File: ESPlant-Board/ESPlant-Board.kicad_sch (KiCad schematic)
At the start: 31 parts, among them J1 Conn_01x05, U1 ESP32-C6-MINI-1/U, U3 Reset, U4 Boot, U5 Temp/Humid-Sensor, U6 Light sensor, U7 AMS1117-3_3, U8 MK-12C02-G025

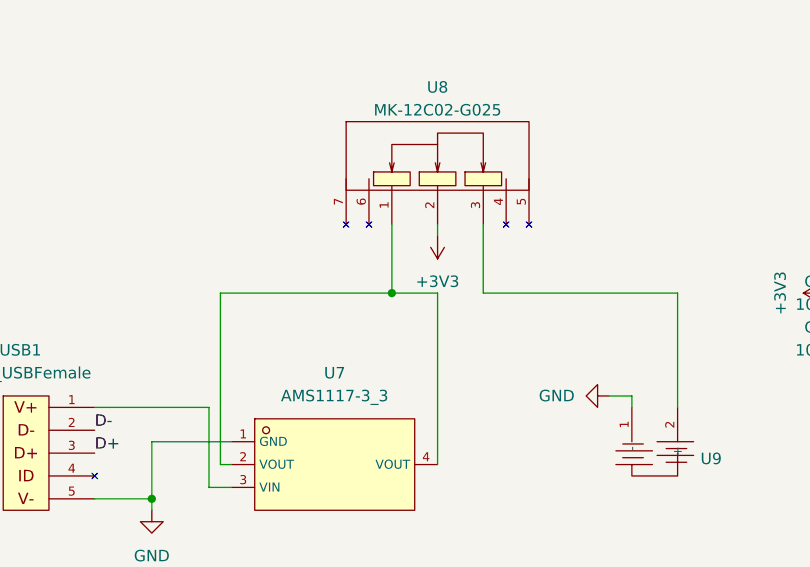
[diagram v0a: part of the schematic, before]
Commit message: Case: Add v2 case with improved folder structure
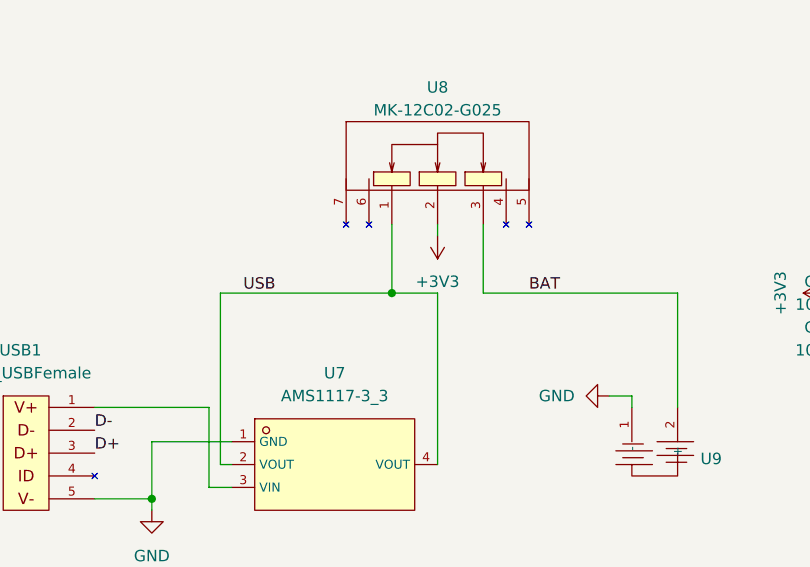
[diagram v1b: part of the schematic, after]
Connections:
- net USB: now reaches U7.2 (VOUT), U7.4 (VOUT), U8.1
- net BAT: now reaches U8.3, U9.2 (+)
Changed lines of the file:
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@@
+    (effects (font (size 1.27 1.27)) (justify left bottom))
+  )
+  (label "USB" (at 48.26 165.1 0) (fields_autoplaced)
     (effects (font (size 1.27 1.27)) (justify left bottom))
   )
@@
     (effects (font (size 1.27 1.27)) (justify right bottom))
   )
+  (label "BAT" (at 80.01 165.1 0) (fields_autoplaced)
+    (effects (font (size 1.27 1.27)) (justify left bottom))
+  )
   (symbol (lib_id "Device:C") (at 74.93 115.57 0) (unit 1)

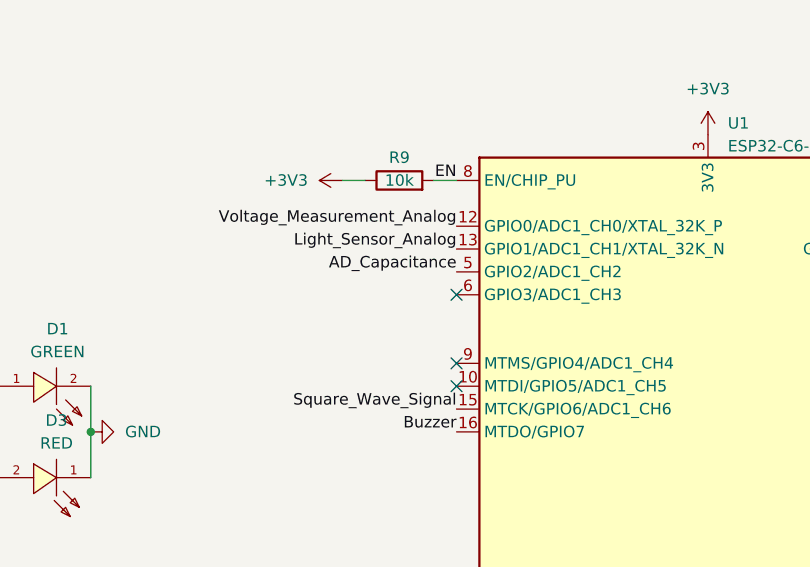
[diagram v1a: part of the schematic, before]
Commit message: Board: Can now differentiate between usb or battery connected
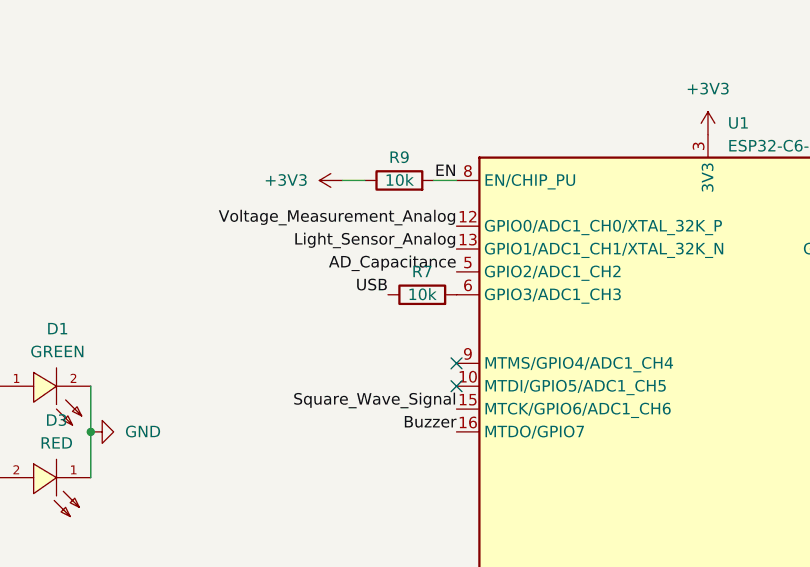
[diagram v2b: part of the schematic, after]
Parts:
- added R7: 10k, Resistor_SMD:R_0402_1005Metric, symbol Device:R
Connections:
- net USB: now also R7.1
- net at U1.6 (GPIO3/ADC1_CH3): now also R7.2
- no-connect marks 7 -> 6
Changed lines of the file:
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@@
   (junction (at 80.01 111.76) (diameter 0) (color 0 0 0 0)
   )
-  (no_connect (at 156.21 82.55))
   (no_connect (at 266.7 88.9))
   (no_connect (at 259.08 58.42))
@@
   (label "EN" (at 280.67 68.58 0) (fields_autoplaced)
     (effects (font (size 1.27 1.27)) (justify left bottom))
+  )
+  (label "USB" (at 148.59 82.55 180) (fields_autoplaced)
+    (effects (font (size 1.27 1.27)) (justify right bottom))
   )
   (label "Voltage_Measurement_Analog" (at 242.57 24.13 0) (fields_autoplaced)
@@
         )
       )
+    )
+  )
+  (symbol (lib_id "Device:R") (at 152.4 82.55 90) (unit 1)
+    (in_bom yes) (on_board yes) (dnp no)
+    (property "Reference" "R7" (at 152.4 80.01 90)
+      (effects (font (size 1.27 1.27)))
+    )
+    (property "Value" "10k" (at 152.4 82.55 90)
+      (effects (font (size 1.27 1.27)))
+    )
+    (property "Footprint" "Resistor_SMD:R_0402_1005Metric" (at 152.4 84.328 90)
+      (effects (font (size 1.27 1.27)) hide)
+    )
+    (property "Datasheet" "~" (at 152.4 82.55 0)
+      (effects (font (size 1.27 1.27)) hide)
+    )
+    (property "LCSC" "C25744" (at 152.4 82.55 0)
+      (effects (font (size 1.27 1.27)) hide)
+    )
+    (property "MPN" "C25744" (at 152.4 82.55 0)
+      (effects (font (size 1.27 1.27)) hide)
+    )
+    (property "JLCPCB Position Offset" "" (at 152.4 82.55 0)
+      (effects (font (size 1.27 1.27)) hide)
+    )
+    (pin "1")
+    (pin "2")
+    (instances
+      (project "ESPlant-Board"
+        (path "/fa2a81f8-bf39-4c28-beef-a6fc807c4564"
+          (reference "R7") (unit 1)
+        )
+      )

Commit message: Board: Update design
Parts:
- added U10, U11, U12, U2: ~, PCM_kikit:Tab_5mm, symbol Custom_Parts:MouseBite5mm
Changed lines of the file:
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@@
+    )
+  )
+  (symbol (lib_id "Custom_Parts:MouseBite5mm") (at 255.27 160.02 0) (unit 1)
+    (in_bom no) (on_board yes) (dnp yes) (fields_autoplaced)
+    (property "Reference" "U10" (at 255.27 158.75 0)
+      (effects (font (size 1.27 1.27)))
+    )
+    (property "Value" "~" (at 255.27 160.02 0)
+      (effects (font (size 1.27 1.27)))
+    )
+    (property "Footprint" "PCM_kikit:Tab_5mm" (at 255.27 160.02 0)
+      (effects (font (size 1.27 1.27)) hide)
+    )
+    (property "Datasheet" "" (at 255.27 160.02 0)
+      (effects (font (size 1.27 1.27)) hide)
+    )
+    (instances
+      (project "ESPlant-Board"
+        (path "/fa2a81f8-bf39-4c28-beef-a6fc807c4564"
+          (reference "U10") (unit 1)
+        )
+      )
     )
   )
@@
     )
   )
+  (symbol (lib_id "Custom_Parts:MouseBite5mm") (at 243.84 160.02 0) (unit 1)
+    (in_bom no) (on_board yes) (dnp yes) (fields_autoplaced)
+    (property "Reference" "U2" (at 243.84 158.75 0)
+      (effects (font (size 1.27 1.27)))
+    )
+    (property "Value" "~" (at 243.84 160.02 0)
+      (effects (font (size 1.27 1.27)))
+    )
+    (property "Footprint" "PCM_kikit:Tab_5mm" (at 243.84 160.02 0)
+      (effects (font (size 1.27 1.27)) hide)
+    )
+    (property "Datasheet" "" (at 243.84 160.02 0)
+      (effects (font (size 1.27 1.27)) hide)
+    )
+    (instances
+      (project "ESPlant-Board"
+        (path "/fa2a81f8-bf39-4c28-beef-a6fc807c4564"
+          (reference "U2") (unit 1)
+        )
+      )
+    )
+  )
   (symbol (lib_id "Custom_Parts:Green-0805-LED") (at 110.49 92.71 180) (unit 1)
     (in_bom yes) (on_board yes) (dnp no) (fields_autoplaced)
@@
         (path "/fa2a81f8-bf39-4c28-beef-a6fc807c4564"
           (reference "#PWR011") (unit 1)
+        )
+      )
+    )
+  )
+  (symbol (lib_id "Custom_Parts:MouseBite5mm") (at 219.71 160.02 0) (unit 1)
+    (in_bom no) (on_board yes) (dnp yes) (fields_autoplaced)
+    (property "Reference" "U11" (at 219.71 158.75 0)
+      (effects (font (size 1.27 1.27)))
+    )
+    (property "Value" "~" (at 219.71 160.02 0)
+      (effects (font (size 1.27 1.27)))
+    )
+    (property "Footprint" "PCM_kikit:Tab_5mm" (at 219.71 160.02 0)
+      (effects (font (size 1.27 1.27)) hide)
+    )
+    (property "Datasheet" "" (at 219.71 160.02 0)
+      (effects (font (size 1.27 1.27)) hide)
+    )
+    (instances
+      (project "ESPlant-Board"
+        (path "/fa2a81f8-bf39-4c28-beef-a6fc807c4564"
+          (reference "U11") (unit 1)
         )
       )
@@
         )
       )
+    )
+  )
+  (symbol (lib_id "Custom_Parts:MouseBite5mm") (at 231.14 160.02 0) (unit 1)
+    (in_bom no) (on_board yes) (dnp yes) (fields_autoplaced)
+    (property "Reference" "U12" (at 231.14 158.75 0)
+      (effects (font (size 1.27 1.27)))
+    )
+    (property "Value" "~" (at 231.14 160.02 0)
+      (effects (font (size 1.27 1.27)))
+    )
+    (property "Footprint" "PCM_kikit:Tab_5mm" (at 231.14 160.02 0)
+      (effects (font (size 1.27 1.27)) hide)
+    )
+    (property "Datasheet" "" (at 231.14 160.02 0)
+      (effects (font (size 1.27 1.27)) hide)
+    )
+    (instances
+      (project "ESPlant-Board"
+        (path "/fa2a81f8-bf39-4c28-beef-a6fc807c4564"
+          (reference "U12") (unit 1)
+        )
+      )

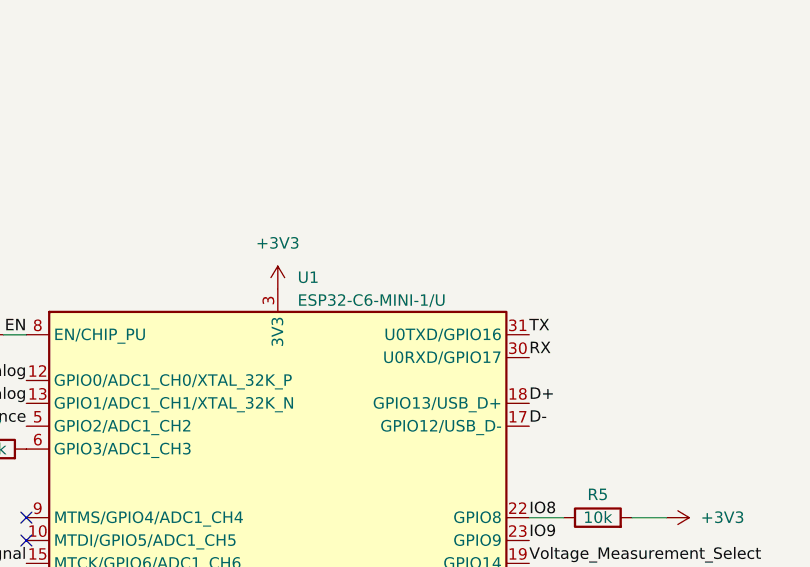
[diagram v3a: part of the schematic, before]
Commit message: Board: Fix library paths
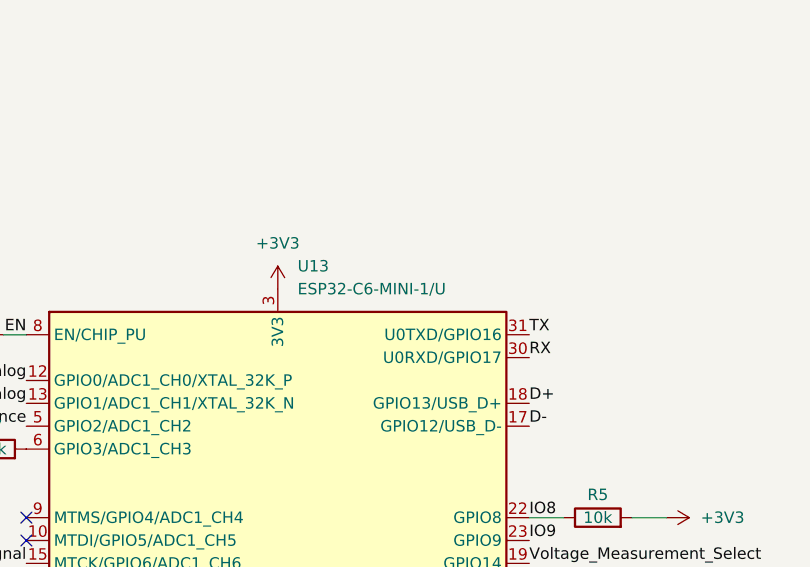
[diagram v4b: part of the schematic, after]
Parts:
- removed U1: ESP32-C6-MINI-1/U, Espressif:ESP32-C6-MINI-1, symbol Espressif:ESP32-C6-MINI-1/U
- added U13: ESP32-C6-MINI-1/U, CustomFootprints:ESP32-C6-MINI-1, symbol Espressif:ESP32-C6-MINI-1/U
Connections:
- net +3V3: now also U13.3 (3V3)
- net AD_Capacitance: now also U13.5 (GPIO2/ADC1_CH2)
- net Buzzer: now also U13.16 (MTDO/GPIO7)
- net D+: now also U13.18 (GPIO13/USB_D+)
- net D-: now also U13.17 (GPIO12/USB_D-)
- net EN: now also U13.8 (EN/CHIP_PU)
- net GND: now also U13.1 (GND), U13.11 (GND), U13.14 (GND), U13.2 (GND), U13.36 (GND), U13.37 (GND), U13.38 (GND), U13.39 (GND), U13.40 (GND), U13.41 (GND), U13.42 (GND), U13.43 (GND), U13.44 (GND), U13.45 (GND), U13.46 (GND), U13.47 (GND), U13.48 (GND), U13.49 (GND), U13.50 (GND), U13.51 (GND), U13.52 (GND), U13.53 (GND)
- net IO8: now also U13.22 (GPIO8)
- net IO9: now also U13.23 (GPIO9)
- net LED_GREEN: now also U13.29 (GPIO23)
- net LED_RED: now also U13.28 (GPIO22)
- net Light_Sensor_Analog: now also U13.13 (GPIO1/ADC1_CH1/XTAL_32K_N)
- net Light_Sensor_In: now also U13.27 (GPIO21)
- net Light_Sensor_Select_1: now also U13.24 (GPIO18)
- net Light_Sensor_Select_2: now also U13.20 (GPIO15)
- net RX: now also U13.30 (U0RXD/GPIO17)
- net Square_Wave_Signal: now also U13.15 (MTCK/GPIO6/ADC1_CH6)
- net TH_SCL: now also U13.26 (GPIO20)
- net TH_SDA: now also U13.25 (GPIO19)
- net TX: now also U13.31 (U0TXD/GPIO16)
- net Voltage_Measurement_Analog: now also U13.12 (GPIO0/ADC1_CH0/XTAL_32K_P)
- net Voltage_Measurement_Select: now also U13.19 (GPIO14)
- net at R7.2: now also U13.6 (GPIO3/ADC1_CH3)
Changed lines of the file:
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@@
     )
   )
-  (symbol (lib_id "Espressif:ESP32-C6-MINI-1/U") (at 184.15 97.79 0) (unit 1)
+  (symbol (lib_name "ESP32-C6-MINI-1/U_1") (lib_id "Espressif:ESP32-C6-MINI-1/U") (at 184.15 97.79 0) (unit 1)
     (in_bom yes) (on_board yes) (dnp no) (fields_autoplaced)
-    (property "Reference" "U1" (at 186.3441 63.5 0)
+    (property "Reference" "U13" (at 186.3441 62.23 0)
       (effects (font (size 1.27 1.27)) (justify left))
     )
-    (property "Value" "ESP32-C6-MINI-1/U" (at 186.3441 66.04 0)
+    (property "Value" "ESP32-C6-MINI-1/U" (at 186.3441 64.77 0)
       (effects (font (size 1.27 1.27)) (justify left))
     )
-    (property "Footprint" "Espressif:ESP32-C6-MINI-1" (at 184.15 142.875 0)
+    (property "Footprint" "CustomFootprints:ESP32-C6-MINI-1" (at 184.15 142.875 0)
       (effects (font (size 1.27 1.27)) hide)
     )
     (property "Datasheet" "https://www.espressif.com/sites/default/files/documentation/esp32-c6-mini-1_datasheet_en.pdf" (at 184.15 146.05 0)
-      (effects (font (size 1.27 1.27)) hide)
-    )
-    (property "LCSC" "C5736265" (at 184.15 97.79 0)
-      (effects (font (size 1.27 1.27)) hide)
-    )
-    (property "MPN" "C5736265" (at 184.15 97.79 0)
       (effects (font (size 1.27 1.27)) hide)
     )
@@
       (project "ESPlant-Board"
         (path "/fa2a81f8-bf39-4c28-beef-a6fc807c4564"
-          (reference "U1") (unit 1)
+          (reference "U13") (unit 1)
         )
       )

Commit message: Board: update
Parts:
- U10, U11, U12, U2: LCSC (none) -> /; MPN (none) -> /
- U13: LCSC (none) -> C5736265; MPN (none) -> C5736265

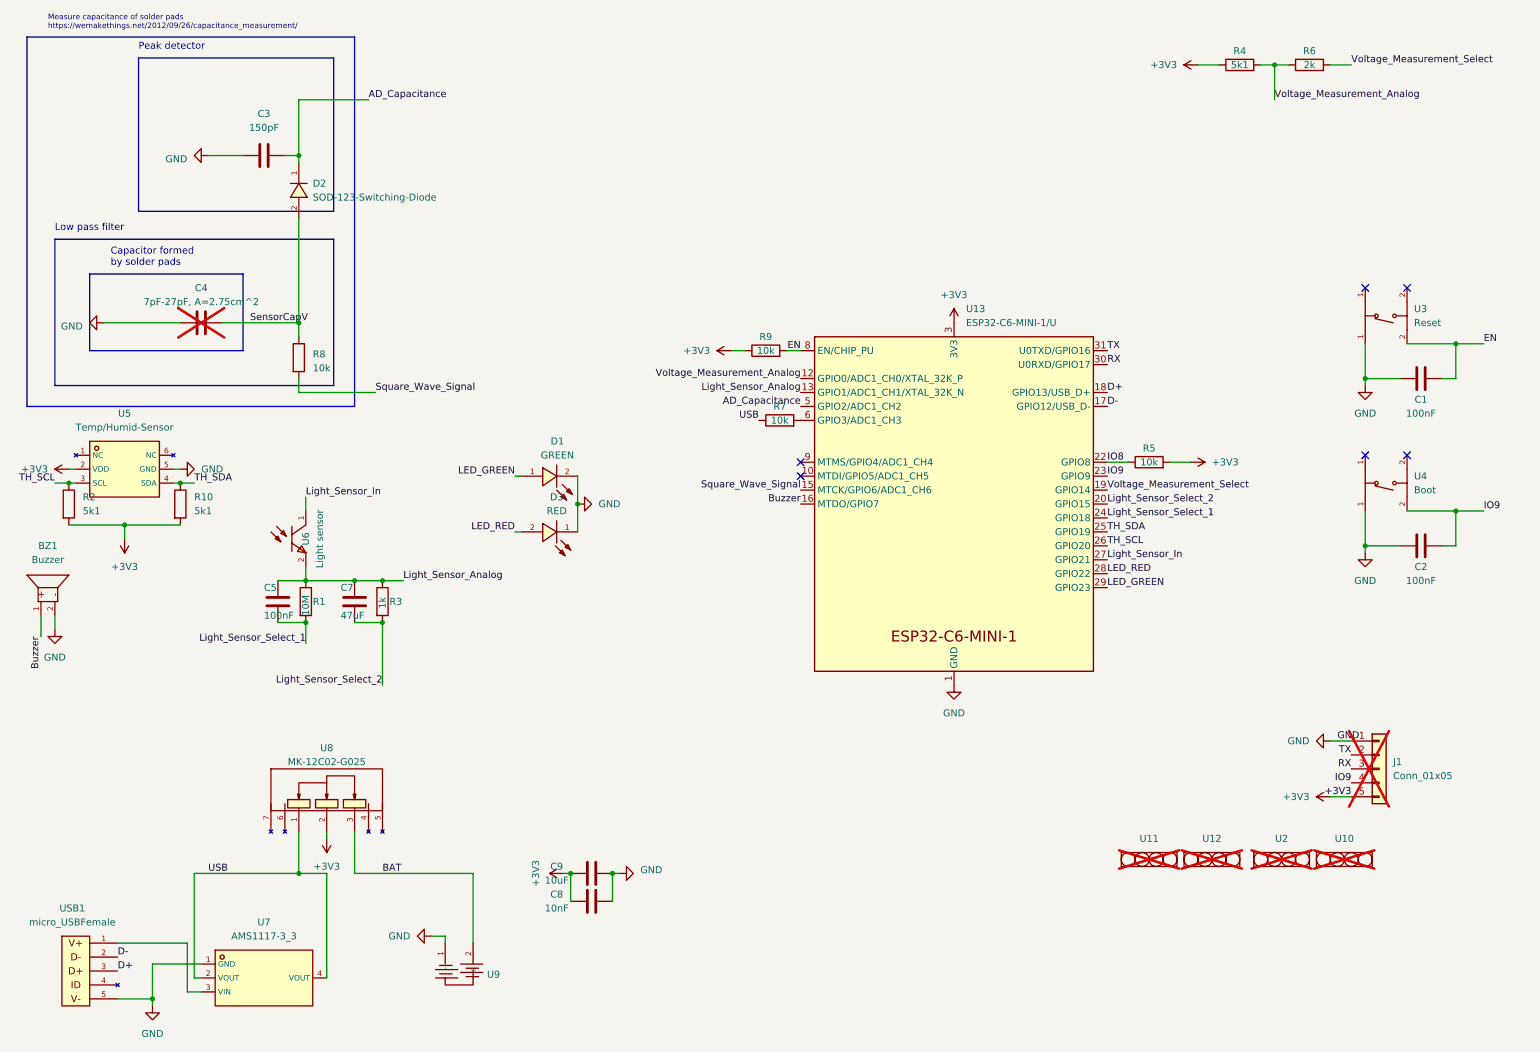
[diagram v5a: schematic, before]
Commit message: Board: Reset KiCad Version to not-nightly
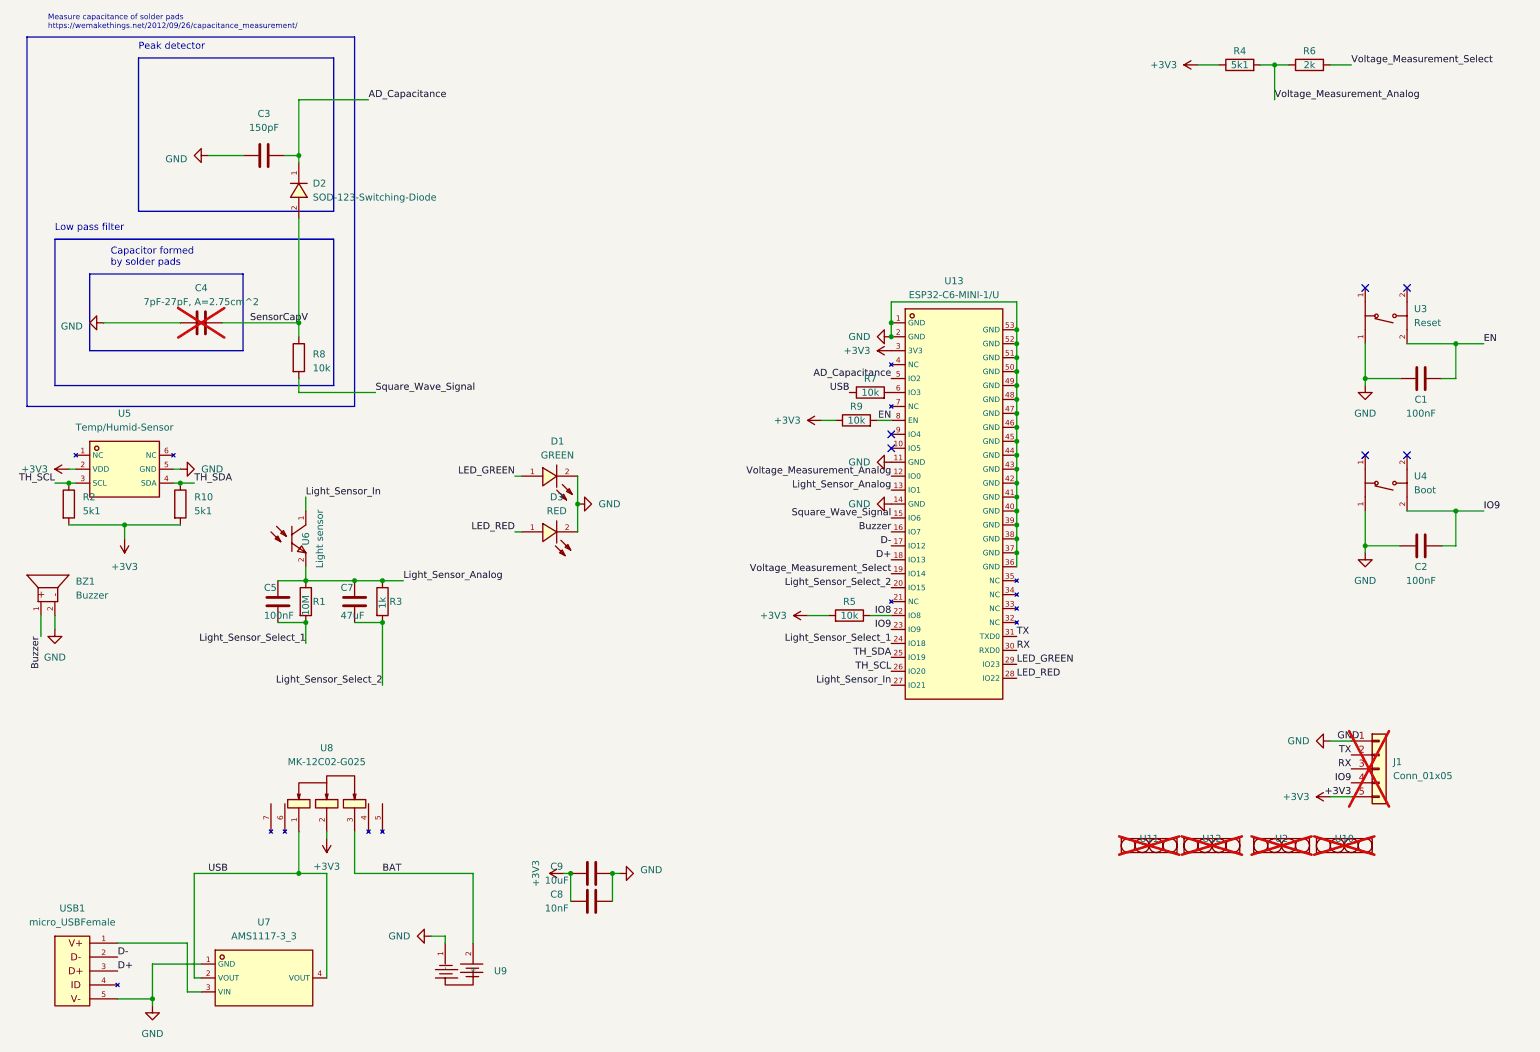
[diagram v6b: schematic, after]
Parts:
- BZ1: symbol Custom_Parts:MLT-8530 -> Custom_Parts:Buzzer
- D1: footprint CustomFootprints:LED0805-GREEN-RD -> CustomFootprints:LED0805-R-RD; symbol Custom_Parts:Green-0805-LED -> Custom_Parts:Led_Green
- D3: footprint CustomFootprints:LED0805-RD_RED -> CustomFootprints:LED0805-R-RD; symbol Custom_Parts:Red-0805-LED -> Custom_Parts:Led_Red
- U10, U11, U12, U2: LCSC / -> (none); MPN / -> (none)
- U13: footprint CustomFootprints:ESP32-C6-MINI-1 -> CustomFootprints:WIFIM-SMD_61P-L16.6-W13.2-P0.80-ESP32-C6-MINI-1-N4; symbol Espressif:ESP32-C6-MINI-1/U -> Custom_Parts:ESP32-C6-MINI-1-N4
- U3, U4: footprint CustomFootprints:SW_Push_1P1T_XKB_TS-1187A -> CustomFootprints:SW-SMD_4P-L5.1-W5.1-P3.70-LS6.5-TL-2; symbol Custom_Parts:TS-1187A-B-A-B -> Custom_Parts:Button
- U6: symbol Custom_Parts:ALS-PT19-315C_L177_TR8 -> Custom_Parts:ALS-PT19-315C_Light_Sensor
- U7: symbol Custom_Parts:AMS1117-3_3 -> Custom_Parts:AMS1117_Voltage_Regulator
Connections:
- net GND: now also D3.2 (-); no longer D3.1 (-)
- net LED_RED: now also D3.1 (+); no longer D3.2 (+)
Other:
- moved on the sheet: R5, R7, R9, U10, U11, U12, U2, USB1
